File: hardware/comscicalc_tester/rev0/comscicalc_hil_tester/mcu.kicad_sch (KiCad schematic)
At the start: 31 parts, among them J1 TSM-110-01-L-DV-A-P-TR, J2 TSM-110-01-L-DV-A-P-TR, U2 W25Q32JVSSIQ, U3 RP2040, Y1 445I23D12M00000

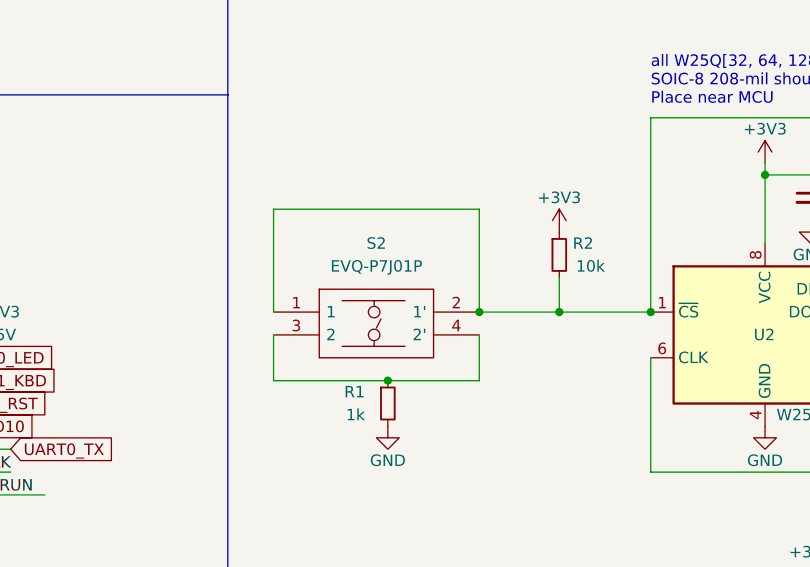
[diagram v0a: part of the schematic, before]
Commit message: Board according to this rev (v2) has been ordered from oshpark.
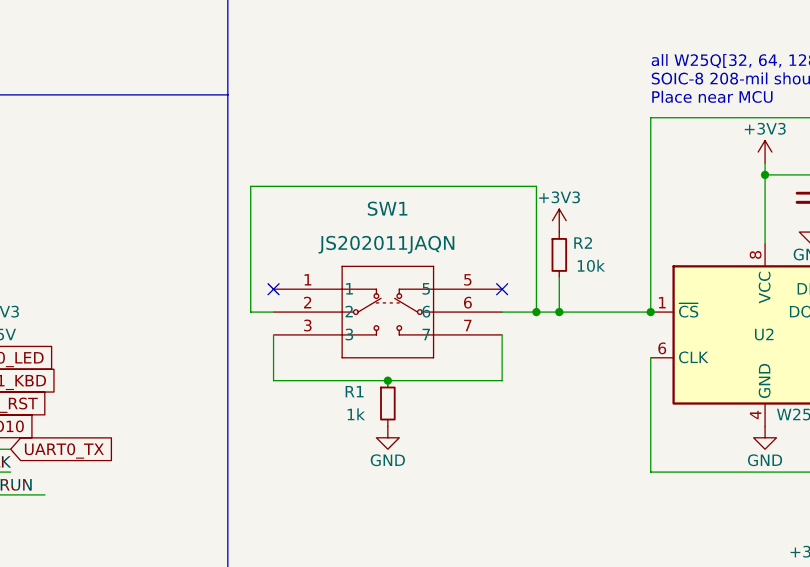
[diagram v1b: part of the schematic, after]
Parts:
- removed S2: EVQ-P7J01P, EVQP7J01P, symbol SamacSys_Parts:EVQ-P7J01P
- added SW1: JS202011JAQN, JS202011JAQN:JS202011JAQN, symbol JS202011JAQN:JS202011JAQN
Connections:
- net QSPI_CSn: now also SW1.2, SW1.6
- net at R1.1: now also SW1.3, SW1.7
- no-connect marks 4 -> 6
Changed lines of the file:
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@@
   (junction (at 46.99 29.21) (diameter 0) (color 0 0 0 0)
   )
-  (junction (at 107.95 80.01) (diameter 0) (color 0 0 0 0)
-  )
   (junction (at 171.45 115.57) (diameter 0) (color 0 0 0 0)
   )
@@
   (junction (at 97.79 87.63) (diameter 0) (color 0 0 0 0)
   )
+  (junction (at 114.3 80.01) (diameter 0) (color 0 0 0 0)
+  )
   (no_connect (at 36.83 100.33))
+  (no_connect (at 85.09 77.47))
   (no_connect (at 254 110.49))
   (no_connect (at 254 107.95))
+  (no_connect (at 110.49 77.47))
   (no_connect (at 49.53 142.24))
   (polyline (pts (xy 13.97 15.24) (xy 80.01 15.24))
@@
     (stroke (width 0) (type default) (color 0 0 0 0))
   )
-  (wire (pts (xy 85.09 80.01) (xy 85.09 68.58))
-    (stroke (width 0) (type default) (color 0 0 0 0))
-  )
   (wire (pts (xy 190.5 82.55) (xy 157.48 82.55))
     (stroke (width 0) (type default) (color 0 0 0 0))
@@
     (stroke (width 0) (type default) (color 0 0 0 0))
   )
+  (wire (pts (xy 82.55 80.01) (xy 85.09 80.01))
+    (stroke (width 0) (type default) (color 0 0 0 0))
+  )
   (wire (pts (xy 191.77 45.72) (xy 191.77 46.99))
     (stroke (width 0) (type default) (color 0 0 0 0))
@@
     (stroke (width 0) (type default) (color 0 0 0 0))
   )
+  (wire (pts (xy 110.49 80.01) (xy 114.3 80.01))
+    (stroke (width 0) (type default) (color 0 0 0 0))
+  )
   (wire (pts (xy 167.64 105.41) (xy 171.45 105.41))
     (stroke (width 0) (type default) (color 0 0 0 0))
@@
     (stroke (width 0) (type default) (color 0 0 0 0))
   )
-  (wire (pts (xy 97.79 87.63) (xy 107.95 87.63))
-    (stroke (width 0) (type default) (color 0 0 0 0))
-  )
   (wire (pts (xy 213.36 54.61) (xy 213.36 45.72))
     (stroke (width 0) (type default) (color 0 0 0 0))
@@
     (stroke (width 0) (type default) (color 0 0 0 0))
   )
-  (wire (pts (xy 85.09 87.63) (xy 97.79 87.63))
+  (wire (pts (xy 97.79 87.63) (xy 110.49 87.63))
     (stroke (width 0) (type default) (color 0 0 0 0))
   )
@@
     (stroke (width 0) (type default) (color 0 0 0 0))
   )
+  (wire (pts (xy 114.3 80.01) (xy 116.84 80.01))
+    (stroke (width 0) (type default) (color 0 0 0 0))
+  )
   (wire (pts (xy 264.16 59.69) (xy 255.27 59.69))
     (stroke (width 0) (type default) (color 0 0 0 0))
@@
     (stroke (width 0) (type default) (color 0 0 0 0))
   )
-  (wire (pts (xy 107.95 80.01) (xy 116.84 80.01))
-    (stroke (width 0) (type default) (color 0 0 0 0))
-  )
   (wire (pts (xy 46.99 29.21) (xy 35.56 29.21))
     (stroke (width 0) (type default) (color 0 0 0 0))
@@
     (stroke (width 0) (type default) (color 0 0 0 0))
   )
-  (wire (pts (xy 85.09 68.58) (xy 107.95 68.58))
-    (stroke (width 0) (type default) (color 0 0 0 0))
-  )
   (wire (pts (xy 58.42 29.21) (xy 69.85 29.21))
     (stroke (width 0) (type default) (color 0 0 0 0))
@@
     (stroke (width 0) (type default) (color 0 0 0 0))
   )
+  (wire (pts (xy 114.3 66.04) (xy 82.55 66.04))
+    (stroke (width 0) (type default) (color 0 0 0 0))
+  )
   (wire (pts (xy 181.61 45.72) (xy 181.61 46.99))
     (stroke (width 0) (type default) (color 0 0 0 0))
@@
     (stroke (width 0) (type default) (color 0 0 0 0))
   )
-  (wire (pts (xy 107.95 87.63) (xy 107.95 82.55))
+  (wire (pts (xy 114.3 80.01) (xy 114.3 66.04))
+    (stroke (width 0) (type default) (color 0 0 0 0))
+  )
+  (wire (pts (xy 110.49 87.63) (xy 110.49 82.55))
     (stroke (width 0) (type default) (color 0 0 0 0))
   )
@@
     (stroke (width 0) (type default) (color 0 0 0 0))
   )
+  (wire (pts (xy 82.55 66.04) (xy 82.55 80.01))
+    (stroke (width 0) (type default) (color 0 0 0 0))
+  )
   (wire (pts (xy 167.64 115.57) (xy 171.45 115.57))
     (stroke (width 0) (type default) (color 0 0 0 0))
@@
     (stroke (width 0) (type default) (color 0 0 0 0))
   )
-  (wire (pts (xy 107.95 68.58) (xy 107.95 80.01))
-    (stroke (width 0) (type default) (color 0 0 0 0))
-  )
   (wire (pts (xy 238.76 44.45) (xy 238.76 45.72))
     (stroke (width 0) (type default) (color 0 0 0 0))
@@
   )
   (wire (pts (xy 160.02 58.42) (xy 160.02 73.66))
+    (stroke (width 0) (type default) (color 0 0 0 0))
+  )
+  (wire (pts (xy 97.79 87.63) (xy 85.09 87.63))
     (stroke (width 0) (type default) (color 0 0 0 0))
   )
@@
     (pin "1")
     (pin "2")
+  )
+  (symbol (lib_id "JS202011JAQN:JS202011JAQN") (at 85.09 77.47 0) (unit 1)
+    (in_bom yes) (on_board yes) (fields_autoplaced)
+    (property "Reference" "SW1" (id 0) (at 97.79 68.58 0)
+      (effects (font (size 1.524 1.524)))
+    )
+    (property "Value" "JS202011JAQN" (id 1) (at 97.79 72.39 0)
+      (effects (font (size 1.524 1.524)))
+    )
+    (property "Footprint" "JS202011JAQN:JS202011JAQN" (id 2) (at 85.09 77.47 0)
+      (effects (font (size 1.27 1.27) italic) hide)
+    )
+    (property "Datasheet" "JS202011JAQN" (id 3) (at 85.09 77.47 0)
+      (effects (font (size 1.27 1.27) italic) hide)
+    )
+    (property "LCSC" "C221664" (id 4) (at 85.09 77.47 0)
+      (effects (font (size 1.27 1.27)) hide)
+    )
+    (pin "1")
+    (pin "2")
+    (pin "3")
+    (pin "5")
+    (pin "6")
+    (pin "7")
   )
   (symbol (lib_id "Device:R_Small") (at 266.7 59.69 90) (unit 1)
@@
     (pin "1")
   )
-  (symbol (lib_id "SamacSys_Parts:EVQ-P7J01P") (at 85.09 80.01 0) (unit 1)
-    (in_bom yes) (on_board yes) (fields_autoplaced)
-    (property "Reference" "S2" (id 0) (at 96.52 72.39 0))
-    (property "Value" "EVQ-P7J01P" (id 1) (at 96.52 74.93 0))
-    (property "Footprint" "EVQP7J01P" (id 2) (at 104.14 77.47 0)
-      (effects (font (size 1.27 1.27)) (justify left) hide)
-    )
-    (property "Datasheet" "https://datasheet.datasheetarchive.com/originals/distributors/Datasheets-DGA6/577750.pdf" (id 3) (at 104.14 80.01 0)
-      (effects (font (size 1.27 1.27)) (justify left) hide)
-    )
-    (property "Description" "Switch,Tactile,3.5x2.9mm,Light Touch Black Side Tactile Switch, SPST 50 mA@ 12 V dc 1.7mm" (id 4) (at 104.14 82.55 0)
-      (effects (font (size 1.27 1.27)) (justify left) hide)
-    )
-    (property "Height" "1" (id 5) (at 104.14 85.09 0)
-      (effects (font (size 1.27 1.27)) (justify left) hide)
-    )
-    (property "Mouser Part Number" "667-EVQP7J01P" (id 6) (at 104.14 87.63 0)
-      (effects (font (size 1.27 1.27)) (justify left) hide)
-    )
-    (property "Mouser Price/Stock" "https://www.mouser.co.uk/ProductDetail/Panasonic/EVQ-P7J01P?qs=rJ%252BziJWpyszkfuBTA00z9w%3D%3D" (id 7) (at 104.14 90.17 0)
-      (effects (font (size 1.27 1.27)) (justify left) hide)
-    )
-    (property "Manufacturer_Name" "Panasonic" (id 8) (at 104.14 92.71 0)
-      (effects (font (size 1.27 1.27)) (justify left) hide)
-    )
-    (property "Manufacturer_Part_Number" "EVQ-P7J01P" (id 9) (at 104.14 95.25 0)
-      (effects (font (size 1.27 1.27)) (justify left) hide)
-    )
-    (pin "1")
-    (pin "2")
-    (pin "3")
-    (pin "4")
-  )
   (symbol (lib_id "power:GND") (at 222.25 156.21 0) (unit 1)
